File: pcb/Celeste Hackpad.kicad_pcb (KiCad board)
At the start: 2 copper layers, 152.4 x 38.1 mm, 29 parts, among them J1 OLED, SW9 EC11, U1 XIAO-RP2040-SMD

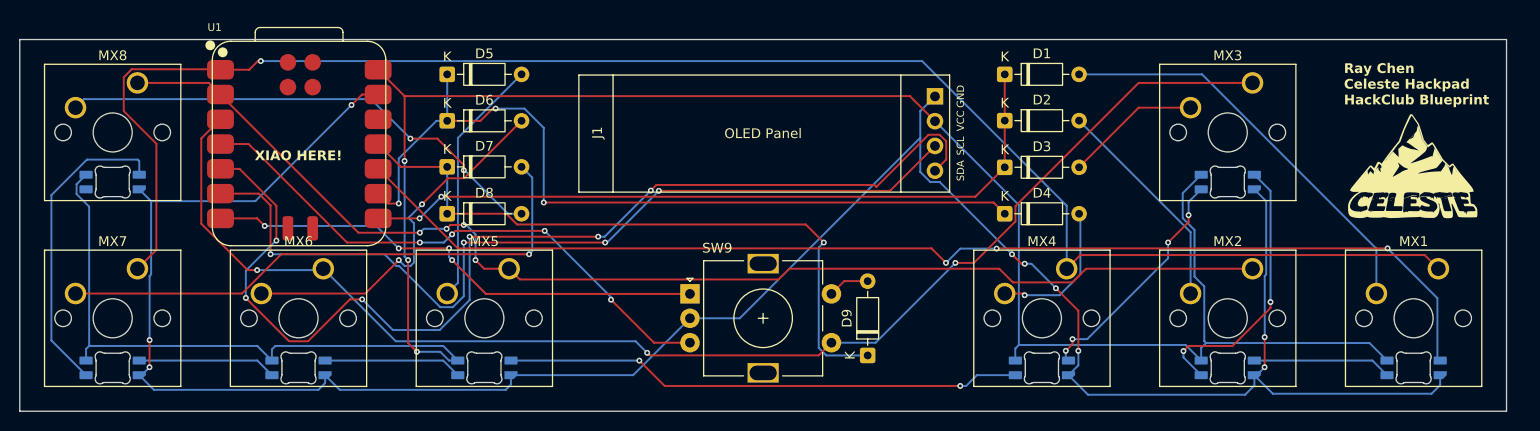
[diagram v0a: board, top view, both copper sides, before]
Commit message: Add ground fill
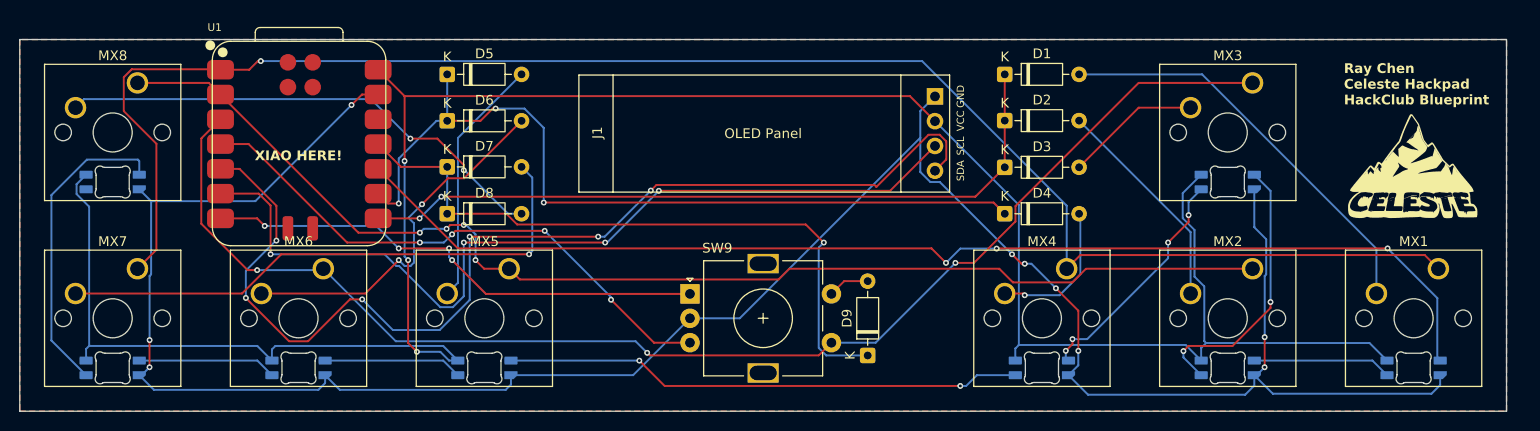
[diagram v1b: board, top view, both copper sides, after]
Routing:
- added copper zone on B.Cu, net GND
- added copper zone on F.Cu, net GND
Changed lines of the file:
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@@
-	)
-	(segment
-		(start 167.0567 63.365914)
-		(end 167.0567 55.8616)
-		(width 0.2)
-		(layer "B.Cu")
-		(net 16)
 	)
 	(segment
@@
 	)
 	(segment
-		(start 167.0567 55.8616)
-		(end 165.8407 54.6456)
+		(start 165.8 58.5)
+		(end 165.8407 58.4593)
 		(width 0.2)
 		(layer "B.Cu")
@@
 	)
 	(segment
+		(start 167.0567 63.365914)
+		(end 167.0567 59.7567)
+		(width 0.2)
+		(layer "B.Cu")
+		(net 16)
+	)
+	(segment
 		(start 73.3 46)
 		(end 63.4384 55.8616)
@@
 	)
 	(segment
+		(start 167.0567 59.7567)
+		(end 165.8 58.5)
+		(width 0.2)
+		(layer "B.Cu")
+		(net 16)
+	)
+	(segment
 		(start 89.6407 73.6956)
 		(end 102.1607 73.6956)
@@
 	)
 	(segment
+		(start 165.8407 58.4593)
+		(end 165.8407 54.6456)
+		(width 0.2)
+		(layer "B.Cu")
+		(net 16)
+	)
+	(segment
 		(start 51.5407 73.6956)
 		(end 51.78047 73.6956)
@@
 		(net 30)
 	)
+	(zone
+		(net 16)
+		(net_name "GND")
+		(layer "F.Cu")
+		(hatch edge 0.5)
+		(connect_pads
+			(clearance 0.5)
+		)
+		(min_thickness 0.25)
+		(filled_areas_thickness no)
+		(fill yes
+			(thermal_gap 0.5)
+			(thermal_bridge_width 0.5)
+		)
+		(polygon
+			(pts
+				(xy 39.290625 39.290625) (xy 39.290625 77.390625) (xy 191.690625 77.390625) (xy 191.690625 39.290625)
+			)
+		)
+	)
+	(zone
+		(net 16)
+		(net_name "GND")
+		(layer "B.Cu")
+		(hatch edge 0.5)
+		(priority 1)
+		(connect_pads
+			(clearance 0.5)
+		)
+		(min_thickness 0.25)
+		(filled_areas_thickness no)
+		(fill yes
+			(thermal_gap 0.5)
+			(thermal_bridge_width 0.5)
+		)
+		(polygon
+			(pts
+				(xy 39.290625 39.290625) (xy 39.290625 77.390625) (xy 191.690625 77.390625) (xy 191.690625 39.290625)
+			)
+		)
+	)
 	(embedded_fonts no)

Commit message: Reset offset of LED
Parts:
- moved LED1 5.08 mm to (182.2, 72.9)
- moved LED2 5.08 mm to (163.1, 72.9)
- moved LED3 5.08 mm to (163.1, 53.9)
- moved LED4 5.08 mm to (144.1, 72.9)
- moved LED5 5.08 mm to (86.9, 72.9)
- moved LED6 5.08 mm to (67.9, 72.9)
- moved LED7 5.08 mm to (48.8, 72.9)
- moved LED8 5.08 mm to (48.8, 53.9)
